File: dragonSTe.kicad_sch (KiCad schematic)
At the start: 0 parts

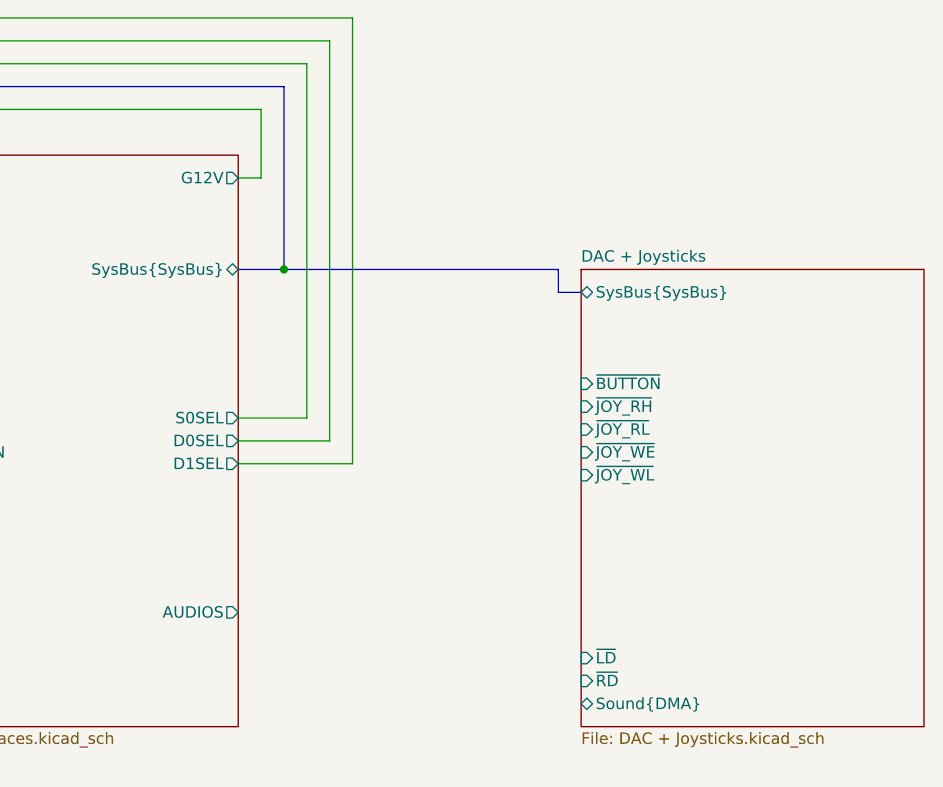
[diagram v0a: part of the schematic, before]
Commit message: motherboard: Added the circuitry for the joystick pads
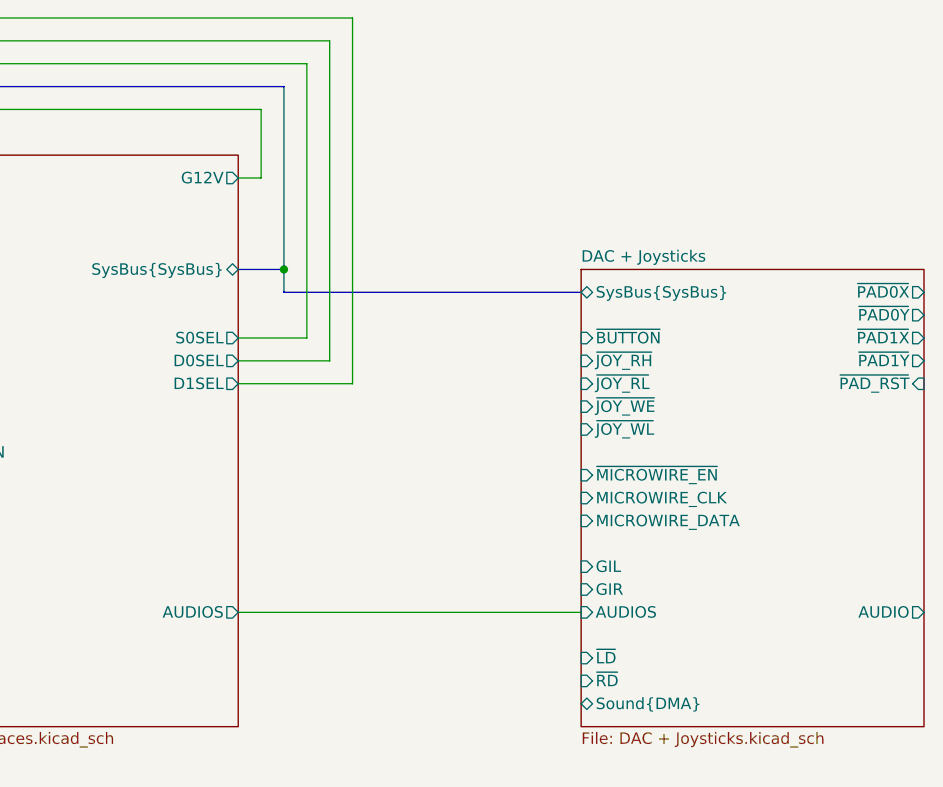
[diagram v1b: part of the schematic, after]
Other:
- sheet DAC + Joysticks ports: added AUDIO, AUDIOS, GIL, GIR, MICROWIRE_CLK, MICROWIRE_DATA, ~{MICROWIRE_EN}, ~{PAD0X}, ~{PAD0Y}, ~{PAD1X}, ~{PAD1Y}, ~{PAD_RST}; removed none

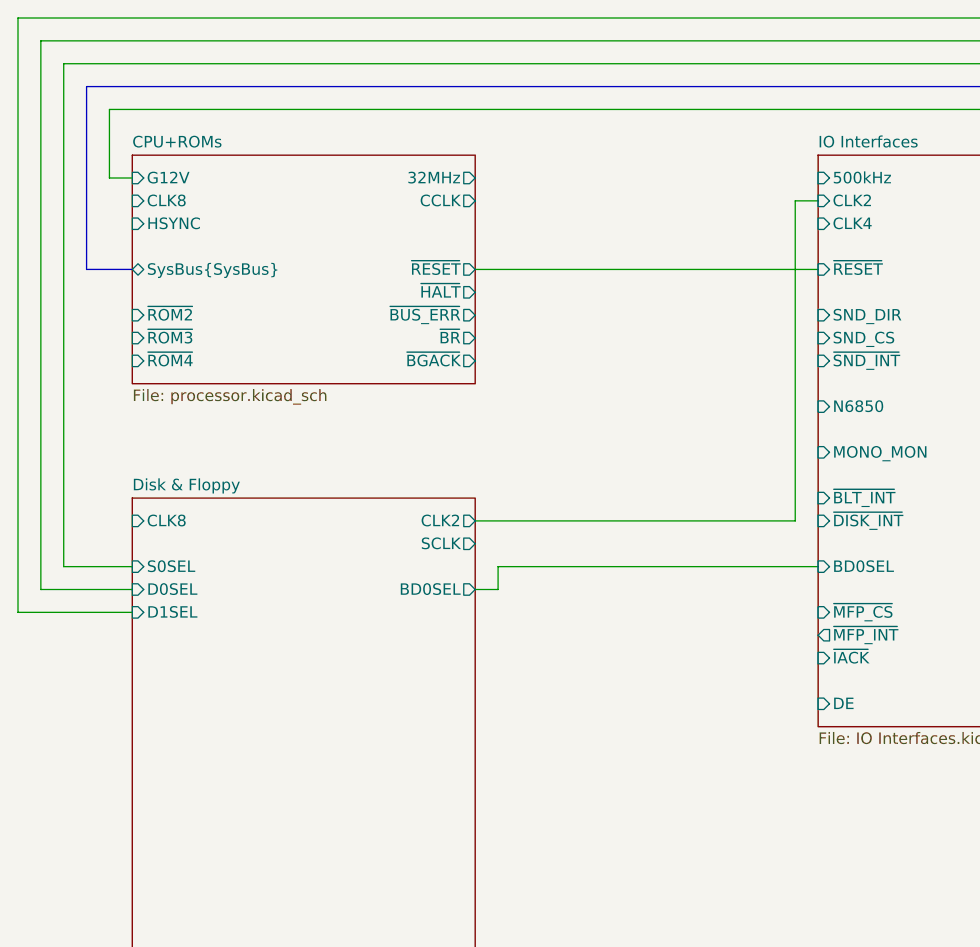
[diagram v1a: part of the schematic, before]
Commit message: motherboard: Added the HDD and FDD controller logic to the schematic
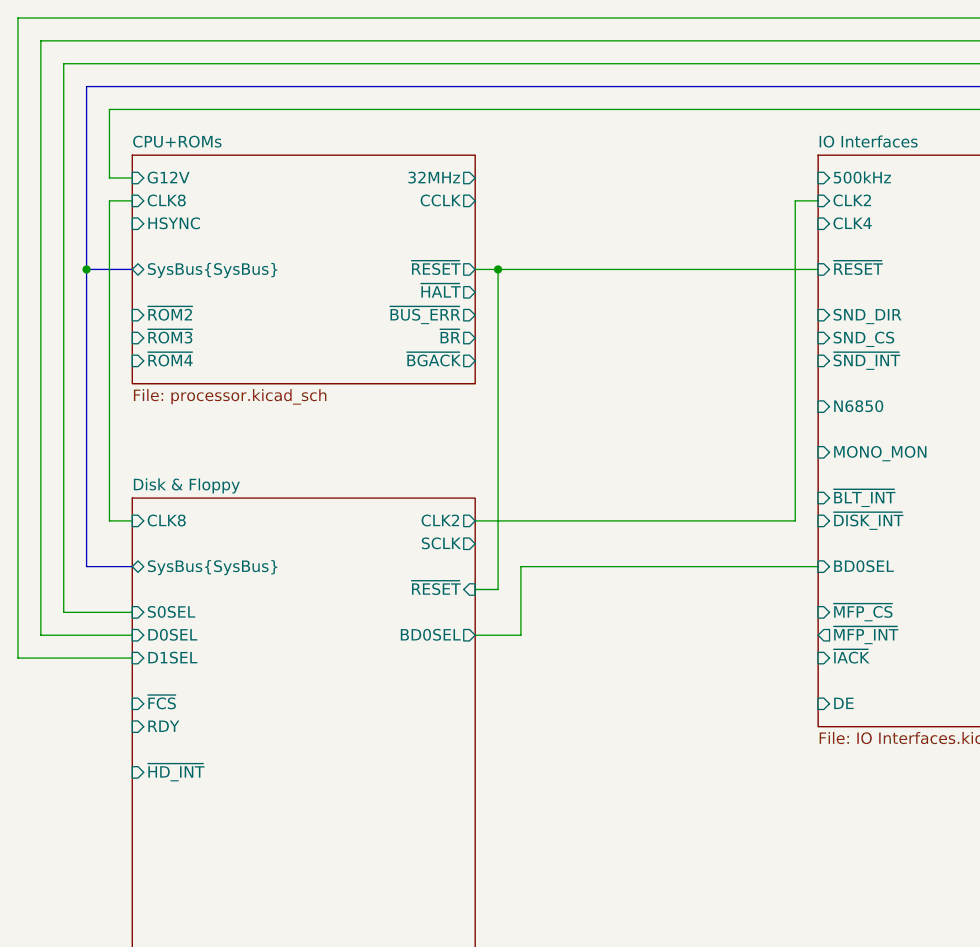
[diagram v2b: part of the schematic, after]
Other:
- sheet Disk & Floppy ports: added RDY, SysBus{SysBus}, ~{FCS}, ~{HD_INT}, ~{RESET}; removed none
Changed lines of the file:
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@@
 	(paper "A4")
+	(junction
+		(at 91.44 76.2)
+		(diameter 0)
+		(color 0 0 0 0)
+	)
+	(junction
+		(at 45.72 76.2)
+		(diameter 0)
+		(color 0 0 0 0)
+	)
 	(junction
 		(at 170.18 76.2)
@@
 	(wire
 		(pts
-			(xy 88.9 76.2) (xy 127 76.2)
-		)
-		(stroke
-			(width 0)
-			(type default)
-		)
-	)
-	(wire
-		(pts
-			(xy 40.64 50.8) (xy 40.64 111.76)
+			(xy 88.9 76.2) (xy 91.44 76.2)
+		)
+		(stroke
+			(width 0)
+			(type default)
+		)
+	)
+	(wire
+		(pts
+			(xy 40.64 50.8) (xy 40.64 116.84)
 		)
 		(stroke
@@
 		)
 	)
+	(bus
+		(pts
+			(xy 50.8 109.22) (xy 45.72 109.22)
+		)
+		(stroke
+			(width 0)
+			(type default)
+		)
+	)
 	(wire
 		(pts
@@
 	(wire
 		(pts
-			(xy 38.1 48.26) (xy 38.1 114.3)
+			(xy 38.1 48.26) (xy 38.1 119.38)
 		)
 		(stroke
@@
 	(wire
 		(pts
+			(xy 88.9 111.76) (xy 91.44 111.76)
+		)
+		(stroke
+			(width 0)
+			(type default)
+		)
+	)
+	(wire
+		(pts
 			(xy 175.26 50.8) (xy 40.64 50.8)
 		)
@@
 		)
 	)
+	(wire
+		(pts
+			(xy 50.8 68.58) (xy 48.26 68.58)
+		)
+		(stroke
+			(width 0)
+			(type default)
+		)
+	)
+	(bus
+		(pts
+			(xy 45.72 109.22) (xy 45.72 76.2)
+		)
+		(stroke
+			(width 0)
+			(type default)
+		)
+	)
 	(bus
 		(pts
@@
 	(wire
 		(pts
-			(xy 91.44 109.22) (xy 91.44 111.76)
-		)
-		(stroke
-			(width 0)
-			(type default)
-		)
-	)
-	(wire
-		(pts
-			(xy 43.18 53.34) (xy 43.18 109.22)
-		)
-		(stroke
-			(width 0)
-			(type default)
-		)
-	)
-	(wire
-		(pts
-			(xy 91.44 111.76) (xy 88.9 111.76)
-		)
-		(stroke
-			(width 0)
-			(type default)
-		)
-	)
-	(wire
-		(pts
-			(xy 127 109.22) (xy 91.44 109.22)
+			(xy 93.98 109.22) (xy 93.98 116.84)
+		)
+		(stroke
+			(width 0)
+			(type default)
+		)
+	)
+	(wire
+		(pts
+			(xy 43.18 53.34) (xy 43.18 114.3)
+		)
+		(stroke
+			(width 0)
+			(type default)
+		)
+	)
+	(wire
+		(pts
+			(xy 48.26 68.58) (xy 48.26 104.14)
+		)
+		(stroke
+			(width 0)
+			(type default)
+		)
+	)
+	(wire
+		(pts
+			(xy 91.44 111.76) (xy 91.44 76.2)
+		)
+		(stroke
+			(width 0)
+			(type default)
+		)
+	)
+	(wire
+		(pts
+			(xy 93.98 116.84) (xy 88.9 116.84)
+		)
+		(stroke
+			(width 0)
+			(type default)
+		)
+	)
+	(wire
+		(pts
+			(xy 127 109.22) (xy 93.98 109.22)
 		)
 		(stroke
@@
 	(wire
 		(pts
-			(xy 38.1 114.3) (xy 50.8 114.3)
-		)
-		(stroke
-			(width 0)
-			(type default)
-		)
-	)
-	(wire
-		(pts
-			(xy 40.64 111.76) (xy 50.8 111.76)
+			(xy 38.1 119.38) (xy 50.8 119.38)
+		)
+		(stroke
+			(width 0)
+			(type default)
+		)
+	)
+	(wire
+		(pts
+			(xy 91.44 76.2) (xy 127 76.2)
+		)
+		(stroke
+			(width 0)
+			(type default)
+		)
+	)
+	(wire
+		(pts
+			(xy 40.64 116.84) (xy 50.8 116.84)
 		)
 		(stroke
@@
 	(wire
 		(pts
+			(xy 48.26 104.14) (xy 50.8 104.14)
+		)
+		(stroke
+			(width 0)
+			(type default)
+		)
+	)
+	(wire
+		(pts
 			(xy 48.26 66.04) (xy 48.26 58.42)
 		)
@@
 	(wire
 		(pts
-			(xy 43.18 109.22) (xy 50.8 109.22)
+			(xy 43.18 114.3) (xy 50.8 114.3)
 		)
 		(stroke
@@
 		)
 		(pin "BD0SEL" output
-			(at 88.9 111.76 0)
+			(at 88.9 116.84 0)
 			(effects
 				(font
@@
 		)
 		(pin "D0SEL" input
-			(at 50.8 111.76 180)
+			(at 50.8 116.84 180)
 			(effects
 				(font
@@
 		)
 		(pin "D1SEL" input
+			(at 50.8 119.38 180)
+			(effects
+				(font
+					(size 1.27 1.27)
+				)
+				(justify left)
+			)
+		)
+		(pin "S0SEL" input
 			(at 50.8 114.3 180)
 			(effects
@@
 			)
 		)
-		(pin "S0SEL" input
+		(pin "SysBus{SysBus}" bidirectional
 			(at 50.8 109.22 180)
 			(effects
 				(font
+					(size 1.27 1.27)
+				)
+				(justify left)
+			)
+		)
+		(pin "~{RESET}" input
+			(at 88.9 111.76 0)
+			(effects
+				(font
+					(size 1.27 1.27)
+				)
+				(justify right)
+			)
+		)
+		(pin "RDY" input
+			(at 50.8 127 180)
+			(effects
+				(font
+					(size 1.27 1.27)
+				)
+				(justify left)
+			)
+		)
+		(pin "~{FCS}" input
+			(at 50.8 124.46 180)
+			(effects
+				(font
+					(size 1.27 1.27)
+				)
+				(justify left)
+			)
+		)
+		(pin "~{HD_INT}" input
+			(at 50.8 132.08 180)
+			(effects
+				(font

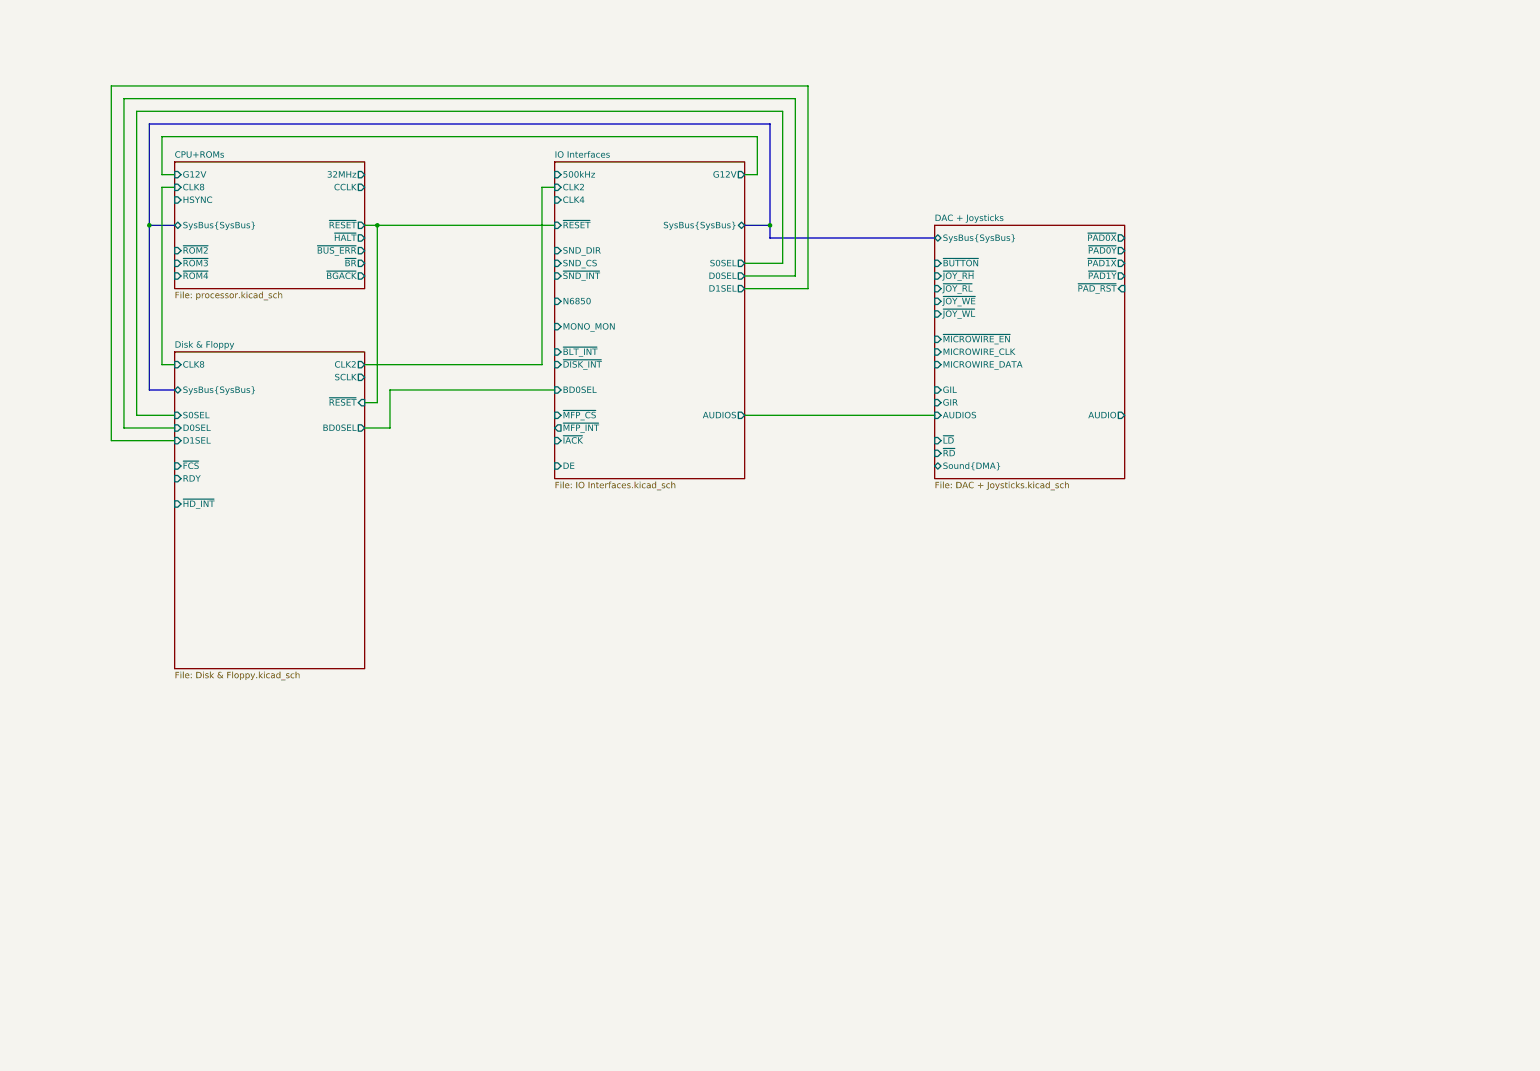
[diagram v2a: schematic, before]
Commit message: motherboard: Added the BLiTTER to the schematic and tidied up a pile
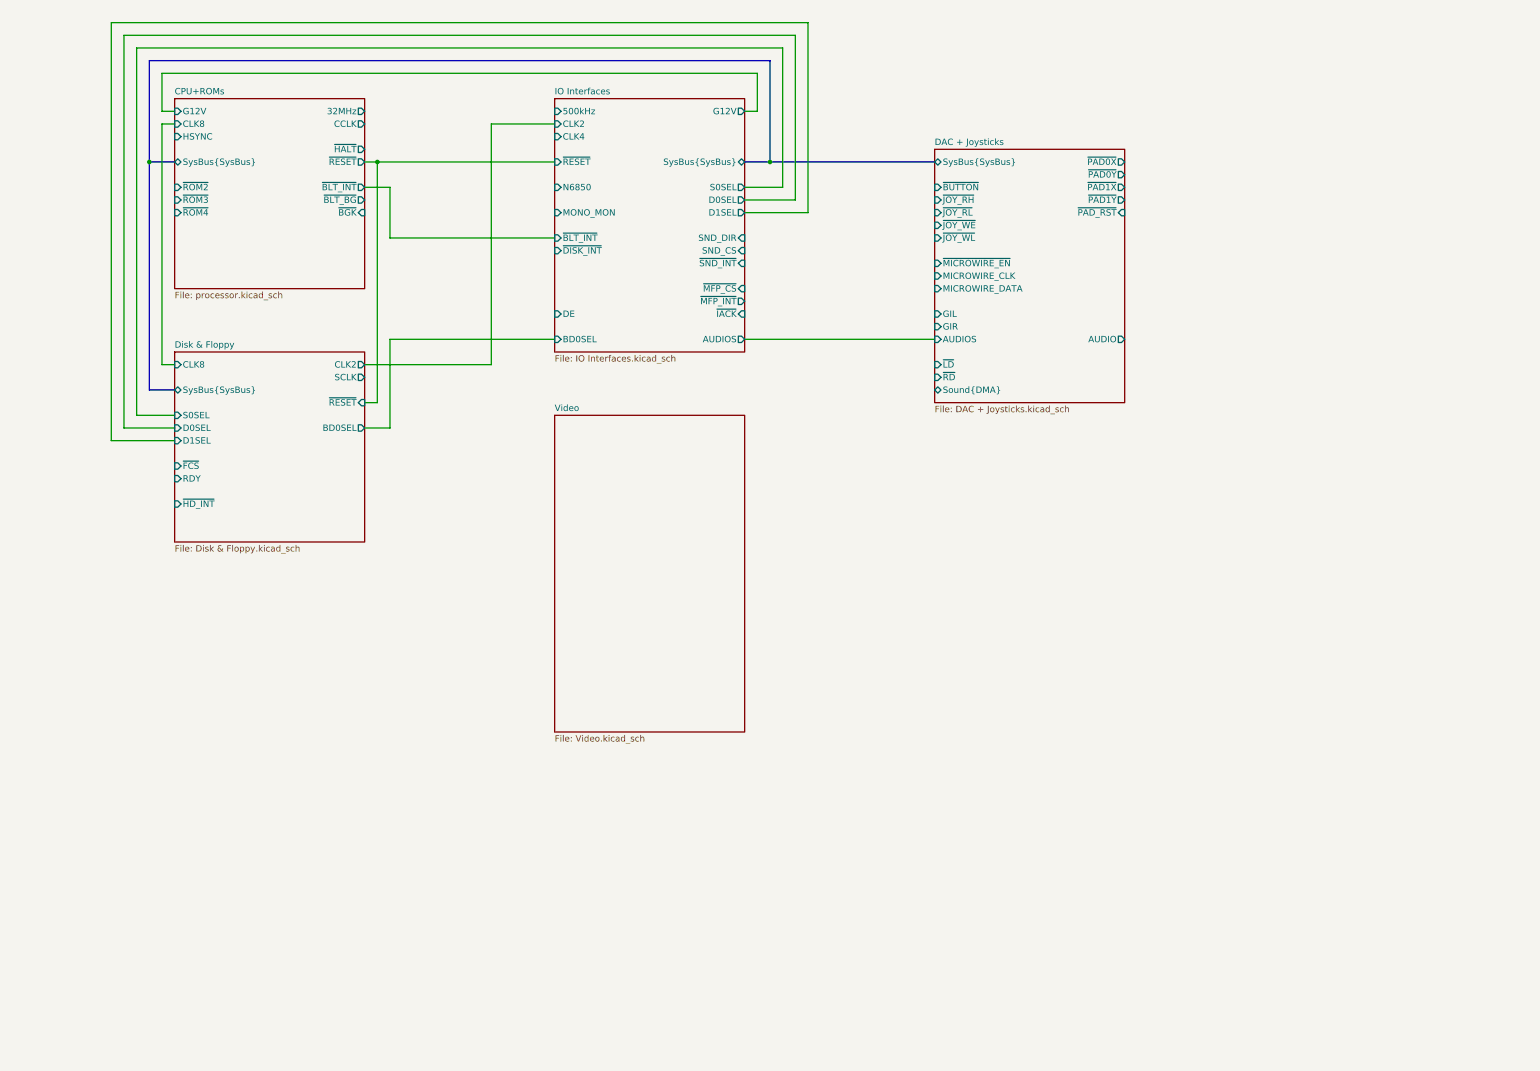
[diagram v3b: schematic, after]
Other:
- added sheet Video (Video.kicad_sch)
- sheet CPU+ROMs ports: added ~{BGK}, ~{BLT_BG}, ~{BLT_INT}; removed ~{BGACK}, ~{BR}, ~{BUS_ERR}
